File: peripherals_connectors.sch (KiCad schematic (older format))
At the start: 26 parts

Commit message: Annotate schematic symbols
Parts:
- gave numbers to parts that had none: 26

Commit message: Assign PCB footprints
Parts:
- C18, C19: footprint (none) -> Library:C_1206
- D3: footprint (none) -> Library:LED_0805
- J10: footprint (none) -> Library:PinHeader_1x14_P2.54mm
- J3: footprint (none) -> Library:PinHeader_2x03_P2.54mm
- J4: footprint (none) -> Library:PinHeader_1x06_P2.54mm
- J5: footprint (none) -> Library:PinHeader_1x03_P2.54mm
- J6, J8, J9: footprint (none) -> Library:PinHeader_1x04_P2.54mm
- J7: footprint (none) -> Library:PinHeader_1x08_P2.54mm
- Q3, Q4, Q5, Q6: footprint Package_TO_SOT_SMD:SOT-23 -> Library:SOT-23
- R17, R18, R19, R20, R21, R22, R23, R24, R25: footprint (none) -> Library:R_1206
- U4, U5: footprint (none) -> Library:SOT-457
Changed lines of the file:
@@
 F 0 "J3" H 2400 1967 50  0000 C CNN
 F 1 "Conn_02x03_Odd_Even" H 2400 1876 50  0000 C CNN
-F 2 "" H 2350 1650 50  0001 C CNN
+F 2 "Library:PinHeader_2x03_P2.54mm" H 2350 1650 50  0001 C CNN
 F 3 "~" H 2350 1650 50  0001 C CNN
 	1    2350 1650
@@
 F 0 "J7" H 6530 1842 50  0000 L CNN
 F 1 "Conn_01x08" H 6530 1751 50  0000 L CNN
-F 2 "" H 6450 1850 50  0001 C CNN
+F 2 "Library:PinHeader_1x08_P2.54mm" H 6450 1850 50  0001 C CNN
 F 3 "~" H 6450 1850 50  0001 C CNN
 	1    6450 1850
@@
 F 0 "J10" H 4530 2142 50  0000 L CNN
 F 1 "Conn_01x14" H 4530 2051 50  0000 L CNN
-F 2 "" H 4450 2150 50  0001 C CNN
+F 2 "Library:PinHeader_1x14_P2.54mm" H 4450 2150 50  0001 C CNN
 F 3 "~" H 4450 2150 50  0001 C CNN
 	1    4450 2150
@@
 F 0 "J8" H 2368 4467 50  0000 C CNN
 F 1 "Conn_01x04" H 2368 4376 50  0000 C CNN
-F 2 "" H 2450 4150 50  0001 C CNN
+F 2 "Library:PinHeader_1x04_P2.54mm" H 2450 4150 50  0001 C CNN
 F 3 "~" H 2450 4150 50  0001 C CNN
 	1    2450 4150
@@
 F 0 "J9" H 2368 5967 50  0000 C CNN
 F 1 "Conn_01x04" H 2368 5876 50  0000 C CNN
-F 2 "" H 2450 5650 50  0001 C CNN
+F 2 "Library:PinHeader_1x04_P2.54mm" H 2450 5650 50  0001 C CNN
 F 3 "~" H 2450 5650 50  0001 C CNN
 	1    2450 5650
@@
 F 0 "C18" H 4215 4296 50  0000 L CNN
 F 1 "100n" H 4215 4205 50  0000 L CNN
-F 2 "" H 4138 4100 50  0001 C CNN
+F 2 "Library:C_1206" H 4138 4100 50  0001 C CNN
 F 3 "~" H 4100 4250 50  0001 C CNN
 	1    4100 4250
@@
 F 0 "C19" H 4215 5796 50  0000 L CNN
 F 1 "100n" H 4215 5705 50  0000 L CNN
-F 2 "" H 4138 5600 50  0001 C CNN
+F 2 "Library:C_1206" H 4138 5600 50  0001 C CNN
 F 3 "~" H 4100 5750 50  0001 C CNN
 	1    4100 5750
@@
 F 0 "U4" H 3400 4567 50  0000 C CNN
 F 1 "74LVC1G58" H 3400 4476 50  0000 C CNN
-F 2 "" H 3400 4250 50  0001 C CNN
+F 2 "Library:SOT-457" H 3400 4250 50  0001 C CNN
 F 3 "http://www.ti.com/lit/sg/scyt129e/scyt129e.pdf" H 3400 4250 50  0001 C CNN
 	1    3400 4250
@@
 F 0 "U5" H 3400 6067 50  0000 C CNN
 F 1 "74LVC1G58" H 3400 5976 50  0000 C CNN
-F 2 "" H 3400 5750 50  0001 C CNN
+F 2 "Library:SOT-457" H 3400 5750 50  0001 C CNN
 F 3 "http://www.ti.com/lit/sg/scyt129e/scyt129e.pdf" H 3400 5750 50  0001 C CNN
 	1    3400 5750
@@
 F 0 "J6" H 9530 1642 50  0000 L CNN
 F 1 "Conn_01x04" H 9530 1551 50  0000 L CNN
-F 2 "" H 9450 1650 50  0001 C CNN
+F 2 "Library:PinHeader_1x04_P2.54mm" H 9450 1650 50  0001 C CNN
 F 3 "~" H 9450 1650 50  0001 C CNN
 	1    9450 1650
@@
 F 0 "Q5" V 8699 1550 50  0000 C CNN
 F 1 "BSS138" V 8790 1550 50  0000 C CNN
-F 2 "Package_TO_SOT_SMD:SOT-23" H 8650 1475 50  0001 L CIN
+F 2 "Library:SOT-23" H 8650 1475 50  0001 L CIN
 F 3 "https://www.onsemi.com/pub/Collateral/BSS138-D.PDF" H 8450 1550 50  0001 L CNN
 	1    8450 1550
@@
 F 0 "Q6" V 8699 2550 50  0000 C CNN
 F 1 "BSS138" V 8790 2550 50  0000 C CNN
-F 2 "Package_TO_SOT_SMD:SOT-23" H 8650 2475 50  0001 L CIN
+F 2 "Library:SOT-23" H 8650 2475 50  0001 L CIN
 F 3 "https://www.onsemi.com/pub/Collateral/BSS138-D.PDF" H 8450 2550 50  0001 L CNN
 	1    8450 2550
@@
 F 0 "R24" H 8820 1446 50  0000 L CNN
 F 1 "10k" H 8820 1355 50  0000 L CNN
-F 2 "" V 8680 1400 50  0001 C CNN
+F 2 "Library:R_1206" V 8680 1400 50  0001 C CNN
 F 3 "~" H 8750 1400 50  0001 C CNN
 	1    8750 1400
@@
 F 0 "R22" H 8220 1446 50  0000 L CNN
 F 1 "10k" H 8220 1355 50  0000 L CNN
-F 2 "" V 8080 1400 50  0001 C CNN
+F 2 "Library:R_1206" V 8080 1400 50  0001 C CNN
 F 3 "~" H 8150 1400 50  0001 C CNN
 	1    8150 1400
@@
 F 0 "R23" H 8220 2446 50  0000 L CNN
 F 1 "10k" H 8220 2355 50  0000 L CNN
-F 2 "" V 8080 2400 50  0001 C CNN
+F 2 "Library:R_1206" V 8080 2400 50  0001 C CNN
 F 3 "~" H 8150 2400 50  0001 C CNN
 	1    8150 2400
@@
 F 0 "R25" H 8820 2446 50  0000 L CNN
 F 1 "10k" H 8820 2355 50  0000 L CNN
-F 2 "" V 8680 2400 50  0001 C CNN
+F 2 "Library:R_1206" V 8680 2400 50  0001 C CNN
 F 3 "~" H 8750 2400 50  0001 C CNN
 	1    8750 2400
@@
 F 0 "J4" H 9530 4242 50  0000 L CNN
 F 1 "Conn_01x06" H 9530 4151 50  0000 L CNN
-F 2 "" H 9450 4250 50  0001 C CNN
+F 2 "Library:PinHeader_1x06_P2.54mm" H 9450 4250 50  0001 C CNN
 F 3 "~" H 9450 4250 50  0001 C CNN
 	1    9450 4250
@@
 F 0 "Q3" V 8699 4150 50  0000 C CNN
 F 1 "BSS138" V 8790 4150 50  0000 C CNN
-F 2 "Package_TO_SOT_SMD:SOT-23" H 8650 4075 50  0001 L CIN
+F 2 "Library:SOT-23" H 8650 4075 50  0001 L CIN
 F 3 "https://www.onsemi.com/pub/Collateral/BSS138-D.PDF" H 8450 4150 50  0001 L CNN
 	1    8450 4150
@@
 F 0 "Q4" V 8699 5150 50  0000 C CNN
 F 1 "BSS138" V 8790 5150 50  0000 C CNN
-F 2 "Package_TO_SOT_SMD:SOT-23" H 8650 5075 50  0001 L CIN
+F 2 "Library:SOT-23" H 8650 5075 50  0001 L CIN
 F 3 "https://www.onsemi.com/pub/Collateral/BSS138-D.PDF" H 8450 5150 50  0001 L CNN
 	1    8450 5150
@@
 F 0 "R19" H 8820 4046 50  0000 L CNN
 F 1 "10k" H 8820 3955 50  0000 L CNN
-F 2 "" V 8680 4000 50  0001 C CNN
+F 2 "Library:R_1206" V 8680 4000 50  0001 C CNN
 F 3 "~" H 8750 4000 50  0001 C CNN
 	1    8750 4000
@@
 F 0 "R17" H 8220 4046 50  0000 L CNN
 F 1 "10k" H 8220 3955 50  0000 L CNN
-F 2 "" V 8080 4000 50  0001 C CNN
+F 2 "Library:R_1206" V 8080 4000 50  0001 C CNN
 F 3 "~" H 8150 4000 50  0001 C CNN
 	1    8150 4000
@@
 F 0 "R20" H 8820 5046 50  0000 L CNN
 F 1 "10k" H 8820 4955 50  0000 L CNN
-F 2 "" V 8680 5000 50  0001 C CNN
+F 2 "Library:R_1206" V 8680 5000 50  0001 C CNN
 F 3 "~" H 8750 5000 50  0001 C CNN
 	1    8750 5000
@@
 F 0 "R18" H 8220 5046 50  0000 L CNN
 F 1 "10k" H 8220 4955 50  0000 L CNN
-F 2 "" V 8080 5000 50  0001 C CNN
+F 2 "Library:R_1206" V 8080 5000 50  0001 C CNN
 F 3 "~" H 8150 5000 50  0001 C CNN
 	1    8150 5000
@@
 F 0 "R21" H 9270 4796 50  0000 L CNN
 F 1 "1k" H 9270 4705 50  0000 L CNN
-F 2 "" V 9130 4750 50  0001 C CNN
+F 2 "Library:R_1206" V 9130 4750 50  0001 C CNN
 F 3 "~" H 9200 4750 50  0001 C CNN
 	1    9200 4750
@@
 F 0 "D3" V 9239 4982 50  0000 R CNN
 F 1 "BLUE LED" V 9148 4982 50  0000 R CNN
-F 2 "" H 9200 5100 50  0001 C CNN
+F 2 "Library:LED_0805" H 9200 5100 50  0001 C CNN
 F 3 "~" H 9200 5100 50  0001 C CNN
 	1    9200 5100
@@
 F 0 "J5" H 9530 6092 50  0000 L CNN
 F 1 "Conn_01x03" H 9530 6001 50  0000 L CNN
-F 2 "" H 9450 6050 50  0001 C CNN
+F 2 "Library:PinHeader_1x03_P2.54mm" H 9450 6050 50  0001 C CNN
 F 3 "~" H 9450 6050 50  0001 C CNN
 	1    9450 6050

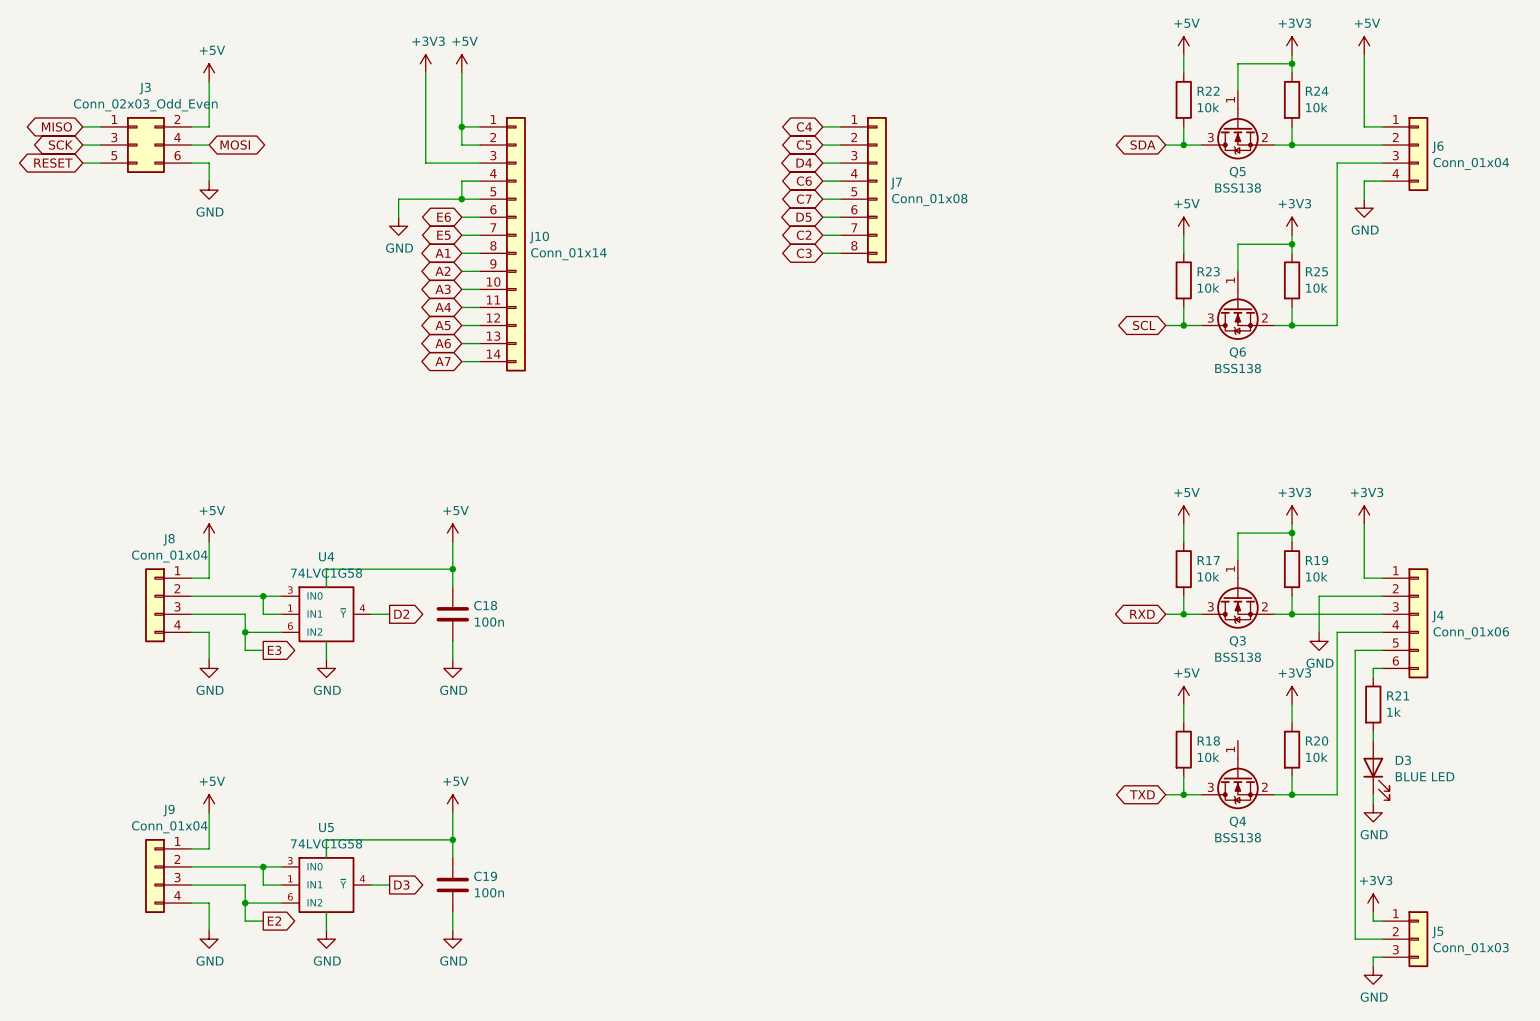
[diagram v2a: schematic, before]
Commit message: Add PCB layout
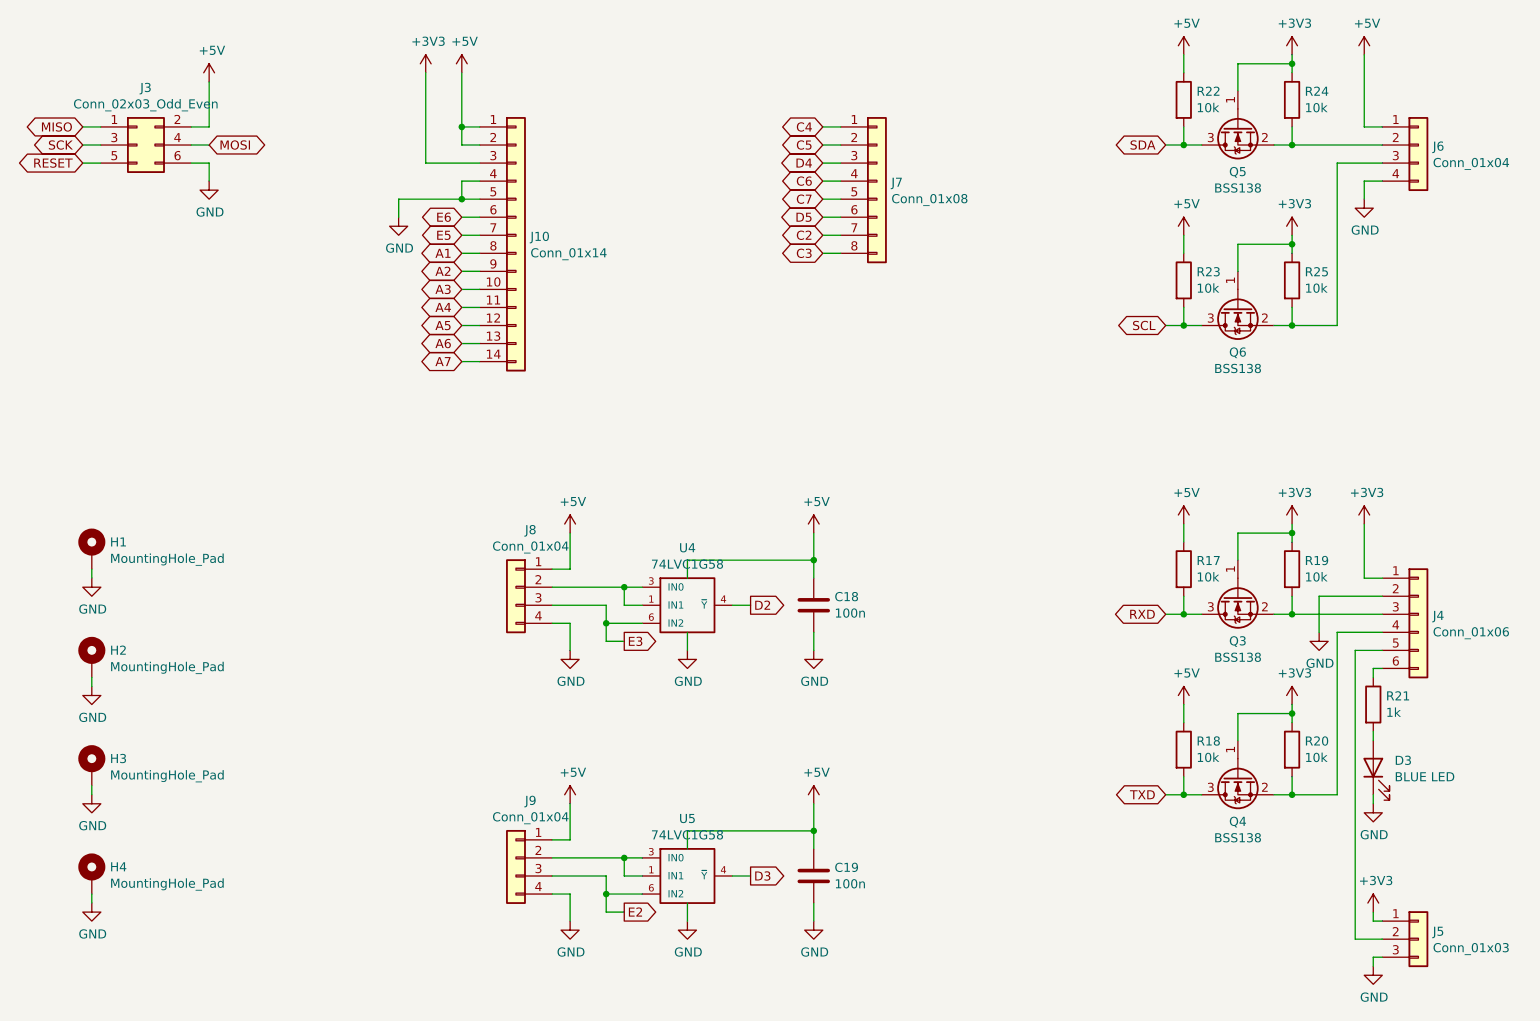
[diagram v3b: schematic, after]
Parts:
- added H1, H2, H3, H4: MountingHole_Pad, MountingHole:MountingHole_3.2mm_M3_ISO7380_Pad, symbol Mechanical:MountingHole_Pad
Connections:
- net +3V3: now also Q4.1 (G)
- net GND: now also H1.1, H2.1, H3.1, H4.1
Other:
- moved on the sheet: C18, C19, J8, J9, U4, U5
